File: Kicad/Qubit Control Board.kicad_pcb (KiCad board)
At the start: 6 copper layers, 144 x 89.5 mm, 149 parts, among them J1 USB_C_Receptacle_PowerOnly_6P, J2 CLK_Pins, J3 Idata, J4 Qdata, J5 SPIdata, J6 SMA, U1 LT3045xMSE, U2 TRF372017IRGZR, U3 LT3045xMSE, U4 LT3045xMSE, U5 SN65LVDS1DBV, U6 AD9743BCPZ, Y1 SiT8008xx-3x-xxN, Y2 CVHD-950-100.000

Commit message: board resize
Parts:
- moved CIN1 8.00 mm to (115.2, 62.5)
- moved CIN2 8.00 mm to (115.8, 66.0)
- moved F1 8.00 mm to (116.8, 58.0)
- moved J1 8.00 mm to (115.3, 39.5)
- moved Rd1 8.00 mm to (115.8, 48.0)
- moved Rd2 8.00 mm to (114.2, 48.0)
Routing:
- net +1.8V: vias 1 -> 4
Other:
- board size 144 x 89.5 mm -> 144 x 81.5 mm
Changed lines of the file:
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@@
 	(footprint "Capacitor_SMD:C_1206_3216Metric_Pad1.33x1.80mm_HandSolder"
 		(layer "F.Cu")
-		(at 115.5 54.5 180)
+		(at 115.25 62.5 180)
 		(descr "Capacitor SMD 1206 (3216 Metric), square (rectangular) end terminal, IPC-7351 nominal with elongated pad for handsoldering. (Body size source: IPC-SM-782 page 76, https://www.pcb-3d.com/wordpress/wp-content/uploads/ipc-sm-782a_amendment_1_and_2.pdf)")
 		(tags "capacitor handsolder")
@@
 	(footprint "Capacitor_SMD:C_0402_1005Metric"
 		(layer "F.Cu")
-		(at 116 58 180)
+		(at 115.75 66 180)
 		(descr "Capacitor SMD 0402 (1005 Metric), square (rectangular) end terminal, IPC-7351 nominal, (Body size source: IPC-SM-782 page 76, https://www.pcb-3d.com/wordpress/wp-content/uploads/ipc-sm-782a_amendment_1_and_2.pdf)")
 		(tags "capacitor")
@@
 	(footprint "Resistor_SMD:R_0603_1608Metric"
 		(layer "F.Cu")
-		(at 116 40 -90)
+		(at 115.75 48 -90)
 		(descr "Resistor SMD 0603 (1608 Metric), square (rectangular) end terminal, IPC-7351 nominal, (Body size source: IPC-SM-782 page 72, https://www.pcb-3d.com/wordpress/wp-content/uploads/ipc-sm-782a_amendment_1_and_2.pdf)")
 		(tags "resistor")
@@
 	(footprint "Fuse:Fuse_1206_3216Metric"
 		(layer "F.Cu")
-		(at 117 50 -90)
+		(at 116.75 58 -90)
 		(descr "Fuse SMD 1206 (3216 Metric), square (rectangular) end terminal, IPC-7351 nominal, (Body size source: http://www.tortai-tech.com/upload/download/2011102023233369053.pdf)")
 		(tags "fuse")
@@
 	(footprint "Resistor_SMD:R_0603_1608Metric"
 		(layer "F.Cu")
-		(at 114.5 40 -90)
+		(at 114.25 48 -90)
 		(descr "Resistor SMD 0603 (1608 Metric), square (rectangular) end terminal, IPC-7351 nominal, (Body size source: IPC-SM-782 page 72, https://www.pcb-3d.com/wordpress/wp-content/uploads/ipc-sm-782a_amendment_1_and_2.pdf)")
 		(tags "resistor")
@@
 	(footprint "Connector_USB:USB_C_Receptacle_GCT_USB4135-GF-A_6P_TopMnt_Horizontal"
 		(layer "F.Cu")
-		(at 115.52 31.4675 180)
+		(at 115.27 39.4675 180)
 		(descr "USB Type C Receptacle, GCT, power-only, 6P, top mounted, horizontal, 3A: https://gct.co/files/drawings/usb4135.pdf")
 		(tags "USB C Type-C Receptacle SMD USB Power-only Charging-only 6P 6C USB4135-GF-A")
@@
 	)
 	(gr_rect
-		(start 106.5 28)
+		(start 106.5 36)
 		(end 250.5 117.5)
 		(stroke
@@
 	)
 	(segment
-		(start 120.59 34.5)
-		(end 121.09 34)
+		(start 120.34 42.5)
+		(end 120.84 42)
 		(width 0.2)
 		(layer "F.Cu")
@@
 	)
 	(segment
-		(start 110.45 34.5)
-		(end 110.395 34.445)
+		(start 110.2 42.5)
+		(end 110.145 42.445)
 		(width 0.2)
 		(layer "F.Cu")
@@
 	)
 	(segment
-		(start 120.59 34.5)
-		(end 120.645 34.445)
+		(start 120.34 42.5)
+		(end 120.395 42.445)
 		(width 0.2)
 		(layer "F.Cu")
@@
 	)
 	(segment
-		(start 118.27 34.5)
-		(end 120.59 34.5)
+		(start 118.02 42.5)
+		(end 120.34 42.5)
 		(width 0.3)
 		(layer "F.Cu")
@@
 	)
 	(via
-		(at 108 31.5)
+		(at 107.75 39.5)
 		(size 0.8)
 		(drill 0.4)
@@
 	)
 	(via
-		(at 116 42.5)
+		(at 115.75 50.5)
 		(size 0.6)
 		(drill 0.3)
@@
 	)
 	(via
-		(at 108.011807 33.947177)
+		(at 107.761807 41.947177)
 		(size 0.8)
 		(drill 0.4)
@@
 	)
 	(via
-		(at 123 30)
+		(at 122.75 38)
 		(size 0.8)
 		(drill 0.4)
@@
 	)
 	(via
-		(at 123 31.5)
+		(at 122.75 39.5)
 		(size 0.8)
 		(drill 0.4)
@@
 	)
 	(via
-		(at 108.011807 30.108976)
+		(at 107.761807 38.108976)
 		(size 0.8)
 		(drill 0.4)
@@
 	)
 	(via
-		(at 123 35.5)
+		(at 122.75 43.5)
 		(size 0.8)
 		(drill 0.4)
@@
 	)
 	(via
-		(at 123 34)
+		(at 122.75 42)
 		(size 0.8)
 		(drill 0.4)
@@
 	)
 	(via
-		(at 114.5 42.5)
+		(at 114.25 50.5)
 		(size 0.6)
 		(drill 0.3)
@@
 	)
 	(via
-		(at 114 56.5)
+		(at 113.75 64.5)
 		(size 0.8)
 		(drill 0.4)
@@
 	)
 	(via
-		(at 108 35.5)
+		(at 107.75 43.5)
 		(size 0.8)
 		(drill 0.4)
@@
 	)
 	(via
-		(at 114.5 58)
+		(at 114.25 66)
 		(size 0.6)
 		(drill 0.3)
@@
 		(net "+1.8V")
 	)
+	(via
+		(at 119.25 79.25)
+		(size 0.6)
+		(drill 0.3)
+		(layers "F.Cu" "B.Cu")
+		(free yes)
+		(net "+1.8V")
+	)
+	(via
+		(at 113.5 76.75)
+		(size 0.6)
+		(drill 0.3)
+		(layers "F.Cu" "B.Cu")
+		(free yes)
+		(net "+1.8V")
+	)
+	(via
+		(at 111.75 75.5)
+		(size 0.6)
+		(drill 0.3)
+		(layers "F.Cu" "B.Cu")
+		(free yes)
+		(net "+1.8V")
+	)
 	(segment
 		(start 108.825 81.5)
@@
 	)
 	(via
-		(at 119 51.5)
+		(at 118.75 59.5)
 		(size 0.8)
 		(drill 0.4)
@@
 	)
 	(via
-		(at 117.5 58)
+		(at 117.25 66)
 		(size 0.6)
 		(drill 0.3)
@@
 	)
 	(via
-		(at 119 54.5)
+		(at 118.75 62.5)
 		(size 0.8)
 		(drill 0.4)
@@
 	)
 	(segment
-		(start 116.02 34.5)
-		(end 116.02 39.155)
+		(start 115.77 42.5)
+		(end 115.77 47.155)
 		(width 0.2)
 		(layer "F.Cu")
@@
 	)
 	(segment
-		(start 116.02 39.155)
-		(end 116 39.175)
+		(start 115.77 47.155)
+		(end 115.75 47.175)
 		(width 0.2)
 		(layer "F.Cu")
@@
 	)
 	(segment
-		(start 112 43.6)
-		(end 117 48.6)
+		(start 111.75 51.6)
+		(end 116.75 56.6)
 		(width 0.45)
 		(layer "F.Cu")
@@
 	)
 	(segment
-		(start 112 38)
-		(end 112 43.6)
+		(start 111.75 46)
+		(end 111.75 51.6)
 		(width 0.45)
 		(layer "F.Cu")
@@
 	)
 	(segment
-		(start 118.5 47)
-		(end 117 48.5)
+		(start 118.25 55)
+		(end 116.75 56.5)
 		(width 0.45)
 		(layer "F.Cu")
@@
 	)
 	(segment
-		(start 118.5 37.5)
-		(end 118.5 47)
+		(start 118.25 45.5)
+		(end 118.25 55)
 		(width 0.45)
 		(layer "F.Cu")
@@
 	)
 	(segment
-		(start 114 36)
-		(end 112 38)
+		(start 113.75 44)
+		(end 111.75 46)
 		(width 0.45)
 		(layer "F.Cu")
@@
 	)
 	(segment
-		(start 117.04 48.56)
-		(end 117 48.6)
+		(start 116.79 56.56)
+		(end 116.75 56.6)
 		(width 0.2)
 		(layer "F.Cu")
@@
 	)
 	(segment
-		(start 117.04 34.5)
-		(end 117.04 36.04)
+		(start 116.79 42.5)
+		(end 116.79 44.04)
 		(width 0.45)
 		(layer "F.Cu")
@@
 	)
 	(segment
-		(start 117 48.5)
-		(end 117 48.6)
+		(start 116.75 56.5)
+		(end 116.75 56.6)
 		(width 0.2)
 		(layer "F.Cu")
@@
 	)
 	(segment
-		(start 117.04 36.04)
-		(end 118.5 37.5)
+		(start 116.79 44.04)
+		(end 118.25 45.5)
 		(width 0.45)
 		(layer "F.Cu")
@@
 	)
 	(segment
-		(start 114 34.5)
-		(end 114 36)
+		(start 113.75 42.5)
+		(end 113.75 44)
 		(width 0.45)
 		(layer "F.Cu")
@@
 	)
 	(segment
-		(start 115.02 34.5)
-		(end 115.02 38.655)
+		(start 114.77 42.5)
+		(end 114.77 46.655)
 		(width 0.2)
 		(layer "F.Cu")
@@
 	)
 	(segment
-		(start 115.02 38.655)
-		(end 114.5 39.175)
+		(start 114.77 46.655)
+		(end 114.25 47.175)
 		(width 0.2)
 		(layer "F.Cu")
@@
 		(polygon
 			(pts
-				(xy 116 53.5) (xy 116 58.5) (xy 113 58.5) (xy 113 53.5)
+				(xy 115.75 61.5) (xy 115.75 66.5) (xy 112.75 66.5) (xy 112.75 61.5)
 			)
 		)
@@
 		(polygon
 			(pts
-				(xy 113.5 29) (xy 113.5 36.5) (xy 107.5 36.5) (xy 107.5 29)
+				(xy 113.25 37) (xy 113.25 44.5) (xy 107.25 44.5) (xy 107.25 37)
 			)
 		)
@@
 		(polygon
 			(pts
-				(xy 123.5 29) (xy 123.5 36.5) (xy 117.5 36.5) (xy 117.5 29)
+				(xy 123.25 37) (xy 123.25 44.5) (xy 117.25 44.5) (xy 117.25 37)
 			)
 		)
@@
 		(polygon
 			(pts
-				(xy 118.5 36) (xy 118.5 48.5) (xy 112 48.5) (xy 112 36)
+				(xy 118.25 44) (xy 118.25 56.5) (xy 111.75 56.5) (xy 111.75 44)
 			)
 		)
@@
 		(polygon
 			(pts
-				(xy 120.5 68.25) (xy 121.75 69.75) (xy 121.75 76) (xy 117.25 76) (xy 117.25 70) (xy 116 68.25) (xy 116 50.5)
-				(xy 120.5 50.5)
+				(xy 120.5 68.25) (xy 121.75 69.75) (xy 121.75 76) (xy 117.25 76) (xy 117.25 70) (xy 116 68.25) (xy 116 58.5)
+				(xy 120.5 58.5)
 			)
 		)
@@
 		(polygon
 			(pts
-				(xy 106.5 28) (xy 250.5 28) (xy 250.5 117.5) (xy 106.5 117.5)
+				(xy 106.5 36) (xy 250.5 36) (xy 250.5 117.5) (xy 106.5 117.5)
 			)
 		)
@@
 		(polygon
 			(pts
-				(xy 110.25 74.5) (xy 124.625 74.5) (xy 124.375 98.5) (xy 115.75 98.5)
+				(xy 117.25 74.5) (xy 124.53395 83.24074) (xy 124.375 98.5) (xy 115.75 98.5) (xy 110.25 74.5)
 			)
 		)

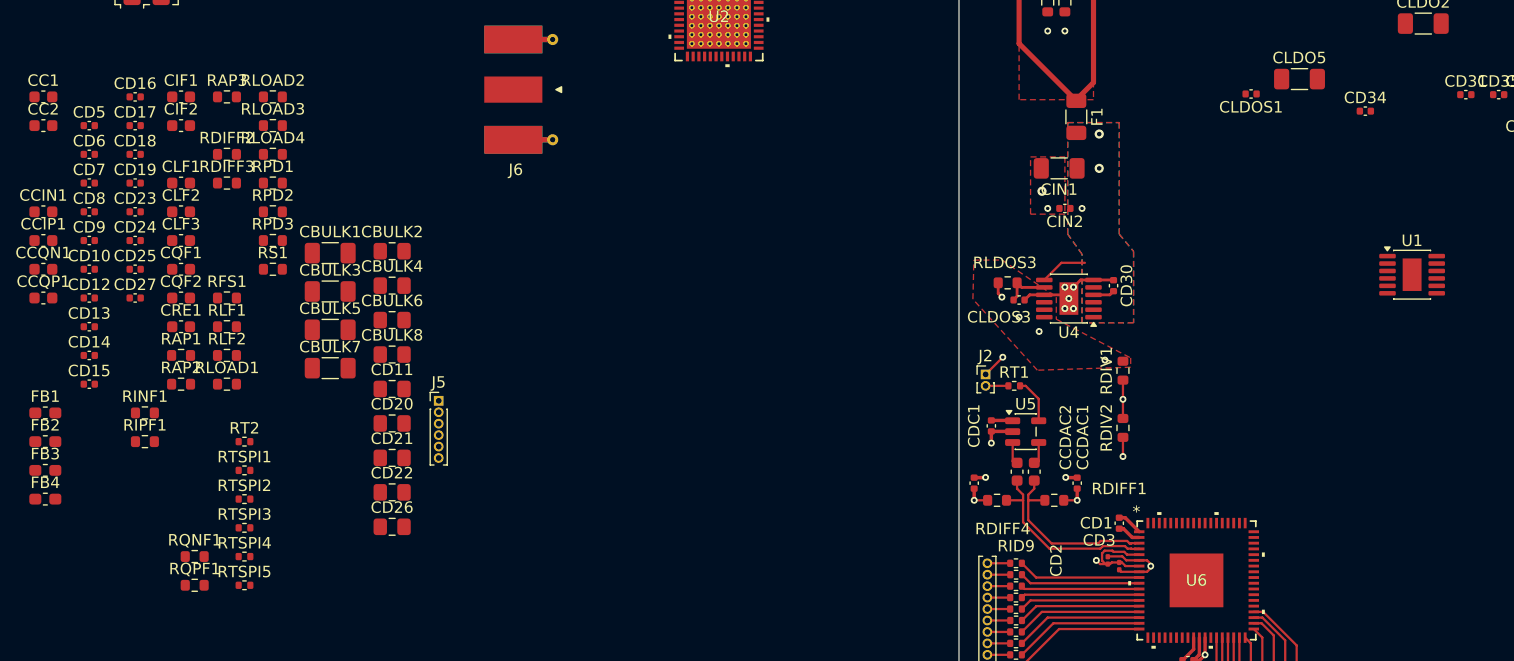
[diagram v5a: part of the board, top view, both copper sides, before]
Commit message: CRC filter routing
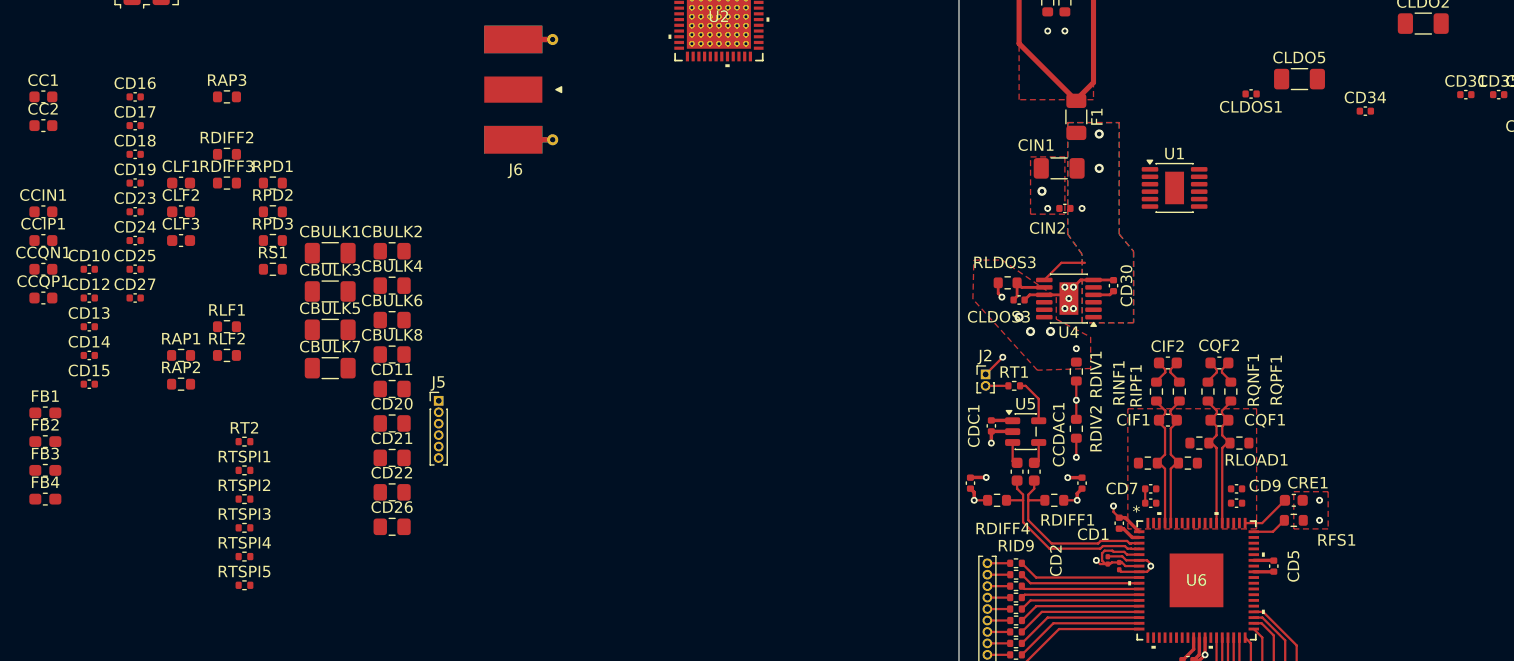
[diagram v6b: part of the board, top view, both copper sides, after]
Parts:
- moved CD5 110.4 mm to (134.0, 97.2), turned to 90 degrees
- moved CD8 103.4 mm to (130.8, 91.8)
- moved CD9 102.6 mm to (130.8, 90.5)
- moved CRE1 98.4 mm to (135.8, 91.5), turned to 180 degrees
- moved CD6 97.2 mm to (123.2, 90.5), turned to 180 degrees
- moved CD7 96.9 mm to (123.2, 91.8), turned to 180 degrees
- moved RFS1 95.2 mm to (135.8, 93.2)
- moved RQPF1 92.1 mm to (130.2, 82.0), turned to 90 degrees
- moved CQF1 91.7 mm to (129.2, 84.5), turned to 180 degrees
- moved CQF2 90.9 mm to (129.2, 79.5), turned to 180 degrees
- moved CIF1 90.7 mm to (124.8, 84.5)
- moved RINF1 90.4 mm to (125.8, 82.0), turned to 90 degrees
- moved RQNF1 89.7 mm to (128.2, 82.0), turned to 90 degrees
- moved RLOAD3 88.9 mm to (131.0, 86.5), turned to 180 degrees
- moved CIF2 88.7 mm to (124.8, 79.5)
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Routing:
- net /IOUTN: track 0.00 -> 11.9 mm
- net /QOUTN: track 0.00 -> 11.9 mm
- net /QOUTP: track 0.00 -> 11.9 mm
- net /IOUTP: track 0.00 -> 11.9 mm
- net Net-(CD28-Pad2): track 21.6 -> 10.4 mm
- net Net-(U6-REFIO): track 0.00 -> 4.30 mm
- net Net-(U6-FSADJ): track 0.00 -> 3.08 mm
- net +1.8V: track 9.61 -> 12.6 mm, vias 4 -> 6
- net GND: track 43.3 -> 45.6 mm, vias 27 -> 29
- net /BBQP: track 0.00 -> 2.22 mm
- net /BBQN: track 0.00 -> 2.22 mm
- net /BBIP: track 0.00 -> 2.22 mm
- net /BBIN: track 0.00 -> 2.22 mm
- net +3.3V-A: track 4.28 -> 5.53 mm

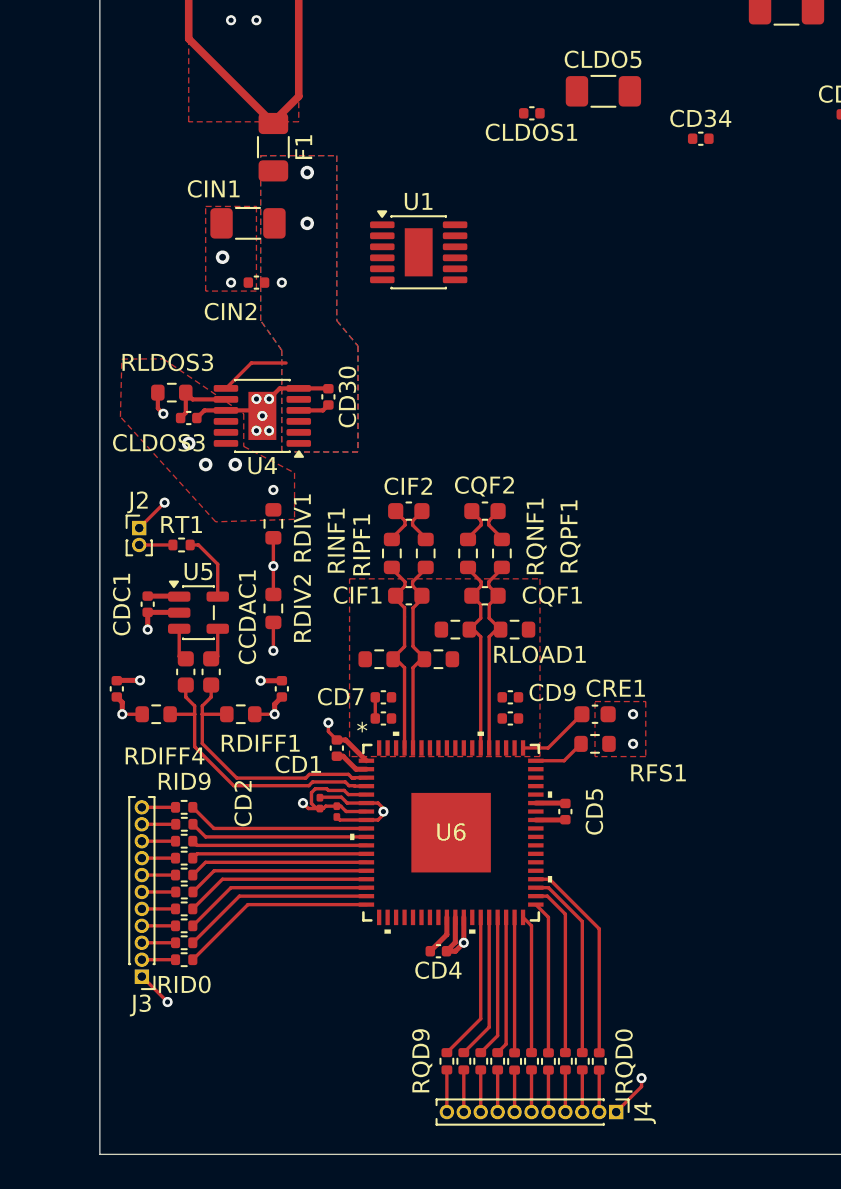
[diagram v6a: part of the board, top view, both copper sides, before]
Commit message: fixed clearance issues
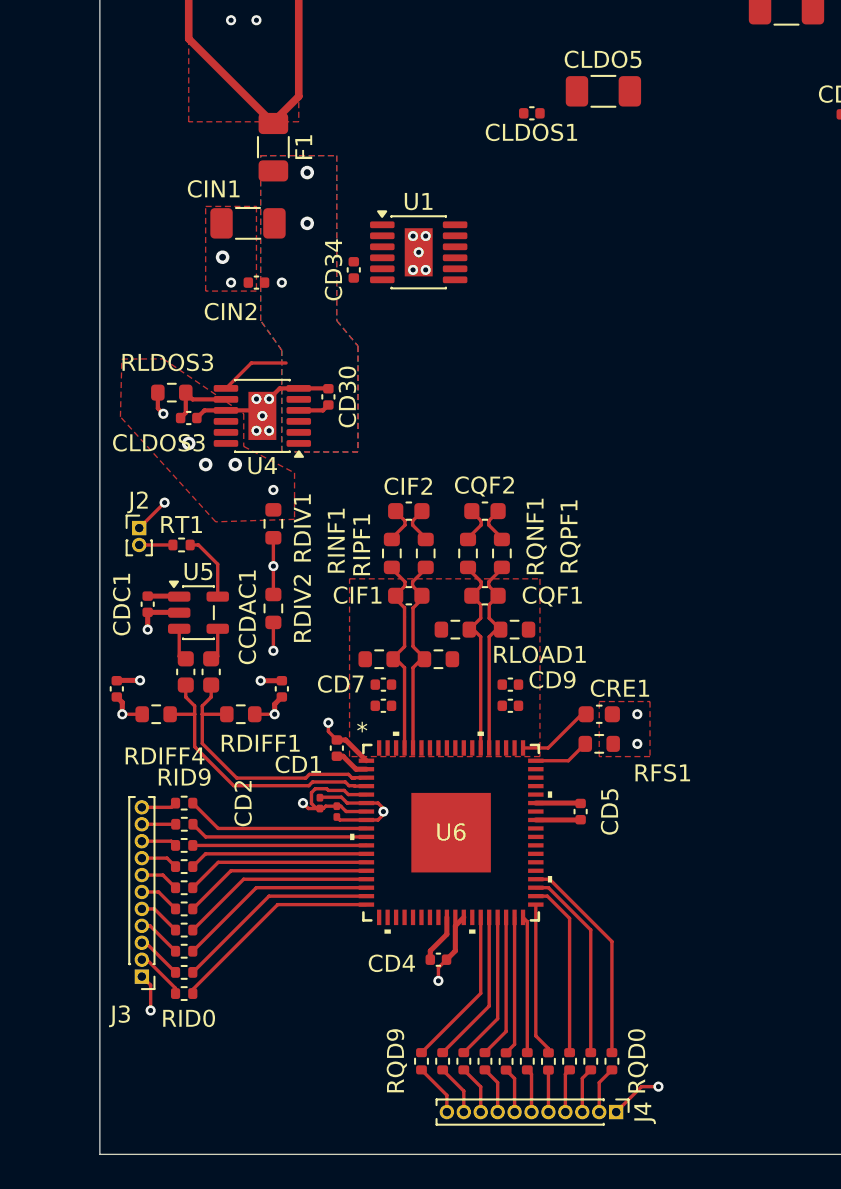
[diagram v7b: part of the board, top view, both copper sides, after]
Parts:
- moved CD34 21.9 mm to (121.5, 65.2), turned to 90 degrees
- moved RID0 2.00 mm to (111.5, 108.0)
- moved RID1 1.75 mm to (111.5, 106.8)
- moved RID2 1.50 mm to (111.5, 105.5)
- moved RQD9 1.50 mm to (125.5, 112.0)
- moved RID3 1.25 mm to (111.5, 104.2)
- moved RQD8 1.25 mm to (126.8, 112.0)
- moved RID4 1.00 mm to (111.5, 103.0)
- moved RQD7 1.00 mm to (128.0, 112.0)
- moved CD5 0.90 mm to (134.9, 97.2)
- moved RQD0 0.75 mm to (136.8, 112.0)
- moved CD6 0.75 mm to (123.2, 89.8)
- moved CD7 0.75 mm to (123.2, 91.0)
- moved CD8 0.75 mm to (130.8, 91.0)
- moved CD9 0.75 mm to (130.8, 89.8)
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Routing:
- net Net-(J3-Pin_2): track 1.99 -> 3.00 mm
- net /ID0: track 11.6 -> 12.6 mm
- net GND: track 45.6 -> 46.5 mm, vias 29 -> 34
- net +1.8V: track 12.6 -> 13.5 mm
- net +3.3V-A: track 5.53 -> 4.78 mm
- net /ID1: track 11.4 -> 12.1 mm
- net Net-(J3-Pin_3): track 1.99 -> 2.71 mm
- net /QD9: track 8.82 -> 9.44 mm
- net /ID2: track 11.2 -> 11.8 mm
- net Net-(J4-Pin_11): track 2.49 -> 3.11 mm
- net Net-(J3-Pin_4): track 1.99 -> 2.61 mm
- net Net-(J4-Pin_10): track 2.49 -> 3.01 mm
- net Net-(J3-Pin_5): track 1.99 -> 2.51 mm
- net /QD8: track 8.61 -> 9.13 mm
- net /ID3: track 11.0 -> 11.5 mm
